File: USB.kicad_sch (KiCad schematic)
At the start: 9 parts, among them U2 AP63200WU

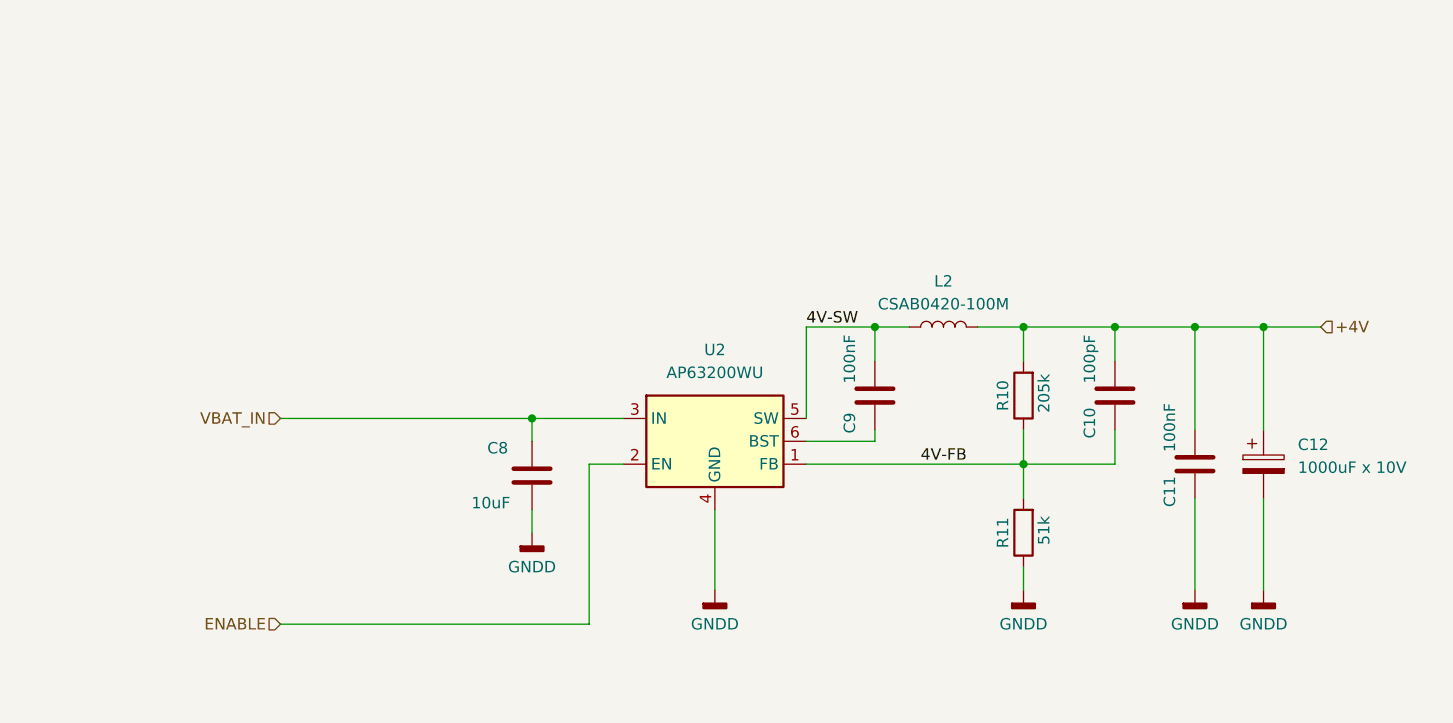
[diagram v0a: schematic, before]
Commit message: Dual SIM version
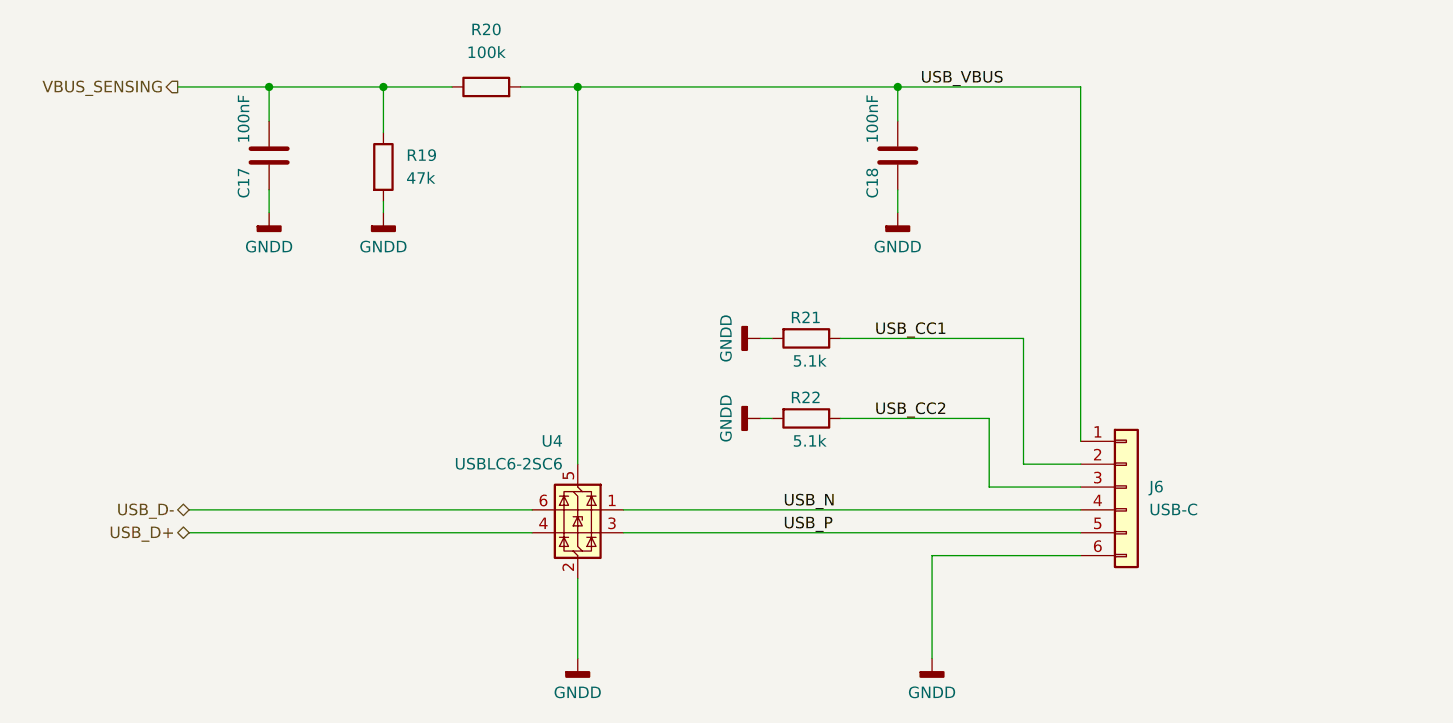
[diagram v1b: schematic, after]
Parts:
- removed C10: 100pF, Capacitor_SMD:C_0805_2012Metric_Pad1.18x1.45mm_HandSolder, symbol Device:C
- removed C11, C9: 100nF, Capacitor_SMD:C_0805_2012Metric_Pad1.18x1.45mm_HandSolder, symbol Device:C
- removed C12: 1000uF x 10V, Capacitor_SMD:CP_Elec_10x10.5, symbol Device:C_Polarized
- removed C8: 10uF, Capacitor_SMD:C_0805_2012Metric_Pad1.18x1.45mm_HandSolder, symbol Device:C
- removed L2: CSAB0420-100M, footprints:CSAB0420-4.4x4.4mm, symbol Device:L
- removed R10: 205k, Resistor_SMD:R_0805_2012Metric_Pad1.20x1.40mm_HandSolder, symbol Device:R
- removed R11: 51k, Resistor_SMD:R_0805_2012Metric_Pad1.20x1.40mm_HandSolder, symbol Device:R
- removed U2: AP63200WU, Package_TO_SOT_SMD:TSOT-23-6, symbol Regulator_Switching:AP63200WU
- added C17, C18: 100nF, Capacitor_SMD:C_0805_2012Metric_Pad1.18x1.45mm_HandSolder, symbol Device:C
- added J6: USB-C, Connector_JST:JST_PH_B6B-PH-K_1x06_P2.00mm_Vertical, symbol Connector_Generic:Conn_01x06
- added R19: 47k, Resistor_SMD:R_0805_2012Metric_Pad1.20x1.40mm_HandSolder, symbol Device:R
- added R20: 100k, Resistor_SMD:R_0805_2012Metric_Pad1.20x1.40mm_HandSolder, symbol Device:R
- added R21, R22: 5.1k, Resistor_SMD:R_0805_2012Metric_Pad1.20x1.40mm_HandSolder, symbol Device:R
- added U4: USBLC6-2SC6, Package_TO_SOT_SMD:SOT-23-6, symbol Power_Protection:USBLC6-2SC6
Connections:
- net GNDD: now also C17.1, C18.1, J6.6 (Pin_6), R19.2, R21.2, R22.2, U4.2 (GND)
- new net USB_CC1: J6.2 (Pin_2), R21.1
- new net USB_CC2: J6.3 (Pin_3), R22.1
- new net USB_D+: U4.4 (I/O2)
- new net USB_D-: U4.6 (I/O1)
- new net USB_N: J6.4 (Pin_4), U4.1 (I/O1)
- new net USB_P: J6.5 (Pin_5), U4.3 (I/O2)
- new net USB_VBUS: C18.2, J6.1 (Pin_1), R20.2, U4.5 (VBUS)
- new net VBUS_SENSING: C17.2, R19.1, R20.1
